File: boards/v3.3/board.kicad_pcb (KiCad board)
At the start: 2 copper layers, 96 x 91.4 mm, 63 parts, among them J1 KF301-2P, J2 KF301-2P, J3 KF301-2P, J4 KF301-2P, J5 KF301-2P, J6 KF301-2P, P1 Pin Header, P2 Pin Header, P3 Pin Header, P4 Pin Header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

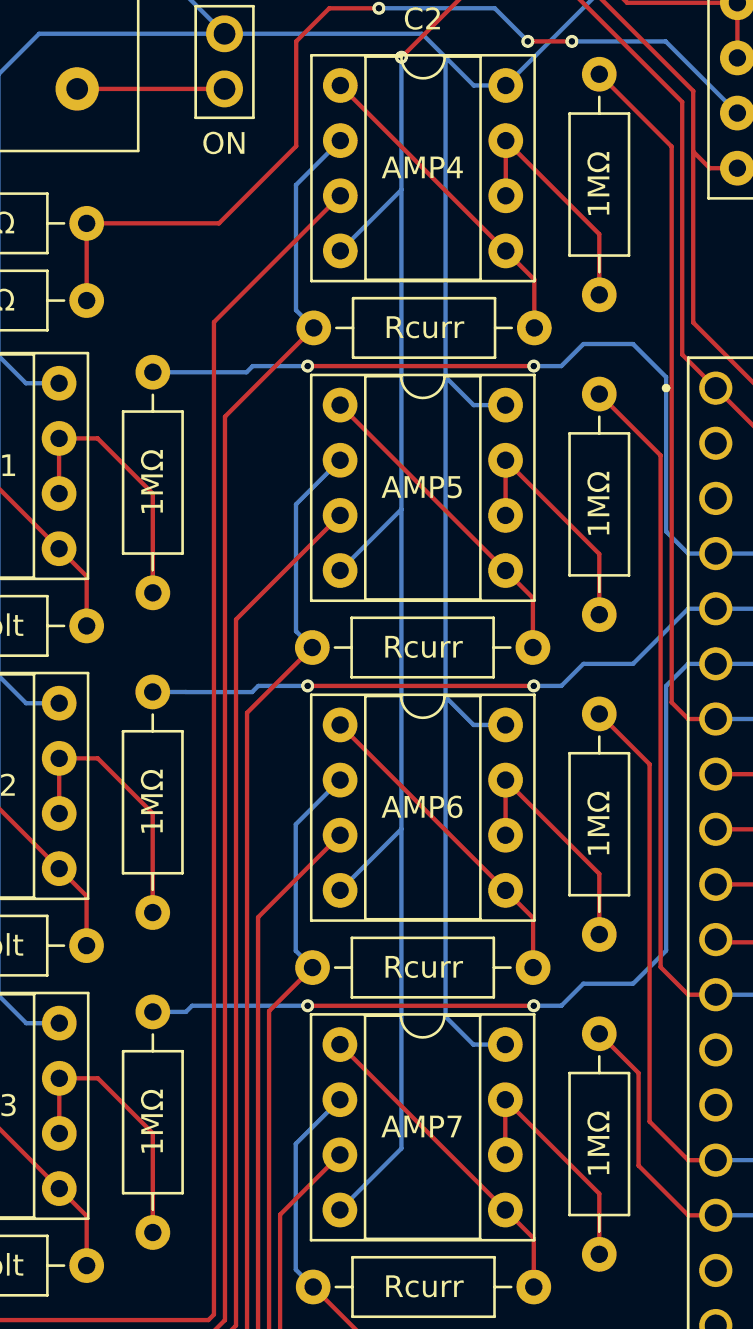
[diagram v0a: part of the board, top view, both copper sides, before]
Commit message: Update the list of components and calcs
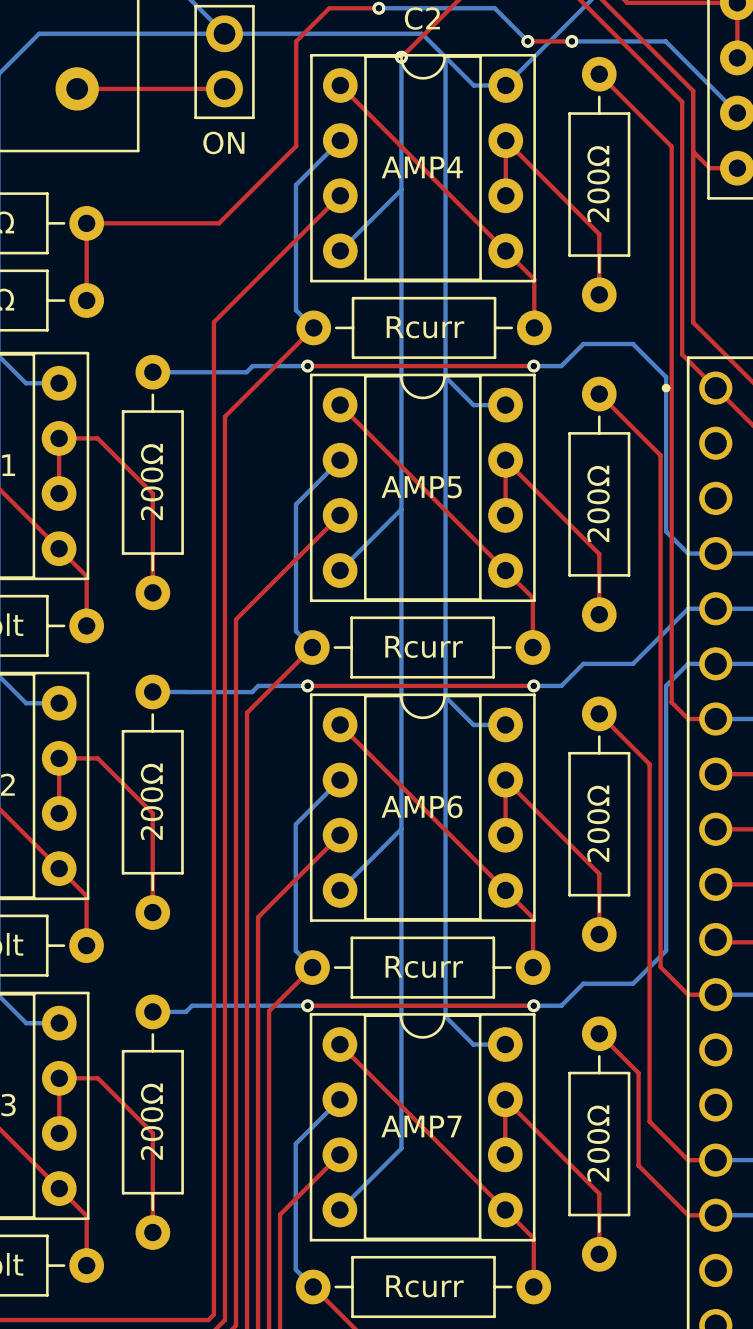
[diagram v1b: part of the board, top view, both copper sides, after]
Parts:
- R13, R14, R15, R16, R17, R18, R19: value 1MΩ -> 200Ω
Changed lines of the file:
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@@
     (title "Energy Guardian V3.3 PCI")
     (date "01/06/2024")
-    (rev "1.0")
+    (rev "1.1")
     (company "linkedin.com/in/lucasrguerra")
     (comment 1 "github.com/lucasrguerra/power_vision")
@@
         (effects (font (size 1 1) (thickness 0.15)))
     )
-    (fp_text value "1MΩ" (at 5.08 2.37 90) (layer "F.Fab") hide
+    (fp_text value "200Ω" (at 5.08 2.37 90) (layer "F.Fab") hide
         (effects (font (size 1 1) (thickness 0.15)))
     )
@@
         (effects (font (size 1 1) (thickness 0.15)))
     )
-    (fp_text value "1MΩ" (at 5.08 2.37 90) (layer "F.Fab") hide
+    (fp_text value "200Ω" (at 5.08 2.37 90) (layer "F.Fab") hide
         (effects (font (size 1 1) (thickness 0.15)))
     )
@@
         (effects (font (size 1 1) (thickness 0.15)))
     )
-    (fp_text value "1MΩ" (at 5.08 2.37 90) (layer "F.Fab") hide
+    (fp_text value "200Ω" (at 5.08 2.37 90) (layer "F.Fab") hide
         (effects (font (size 1 1) (thickness 0.15)))
     )
@@
         (effects (font (size 1 1) (thickness 0.15)))
     )
-    (fp_text value "1MΩ" (at 5.08 2.37 90) (layer "F.Fab") hide
+    (fp_text value "200Ω" (at 5.08 2.37 90) (layer "F.Fab") hide
         (effects (font (size 1 1) (thickness 0.15)))
     )
@@
         (effects (font (size 1 1) (thickness 0.15)))
     )
-    (fp_text value "1MΩ" (at 5.08 2.37 90) (layer "F.Fab") hide
+    (fp_text value "200Ω" (at 5.08 2.37 90) (layer "F.Fab") hide
         (effects (font (size 1 1) (thickness 0.15)))
     )
@@
         (effects (font (size 1 1) (thickness 0.15)))
     )
-    (fp_text value "1MΩ" (at 5.08 2.37 90) (layer "F.Fab") hide
+    (fp_text value "200Ω" (at 5.08 2.37 90) (layer "F.Fab") hide
         (effects (font (size 1 1) (thickness 0.15)))
     )
@@
         (effects (font (size 1 1) (thickness 0.15)))
     )
-    (fp_text value "1MΩ" (at 5.08 2.37 90) (layer "F.Fab") hide
+    (fp_text value "200Ω" (at 5.08 2.37 90) (layer "F.Fab") hide
         (effects (font (size 1 1) (thickness 0.15)))
     )

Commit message: Update board v3.3
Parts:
- moved P2 0.25 mm to (161.3, 56.9)
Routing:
- net TP B-1: track 17.3 -> 18.5 mm
- net MISO: track 33.0 -> 32.3 mm, vias 2 -> 1
- net Vcc: track 157.8 -> 158.4 mm
- net GND: track 319.4 -> 320.0 mm
- net CS: track 35.4 -> 34.8 mm, vias 2 -> 1

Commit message: Add the earth plan in the v3.3 board
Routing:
- net GND: track 320.0 -> 0.18 mm, vias 1 -> 0
- net Vcc: track 158.4 -> 172.2 mm
- added copper zone on B.Cu, net GND
- added copper zone on F.Cu, net GND

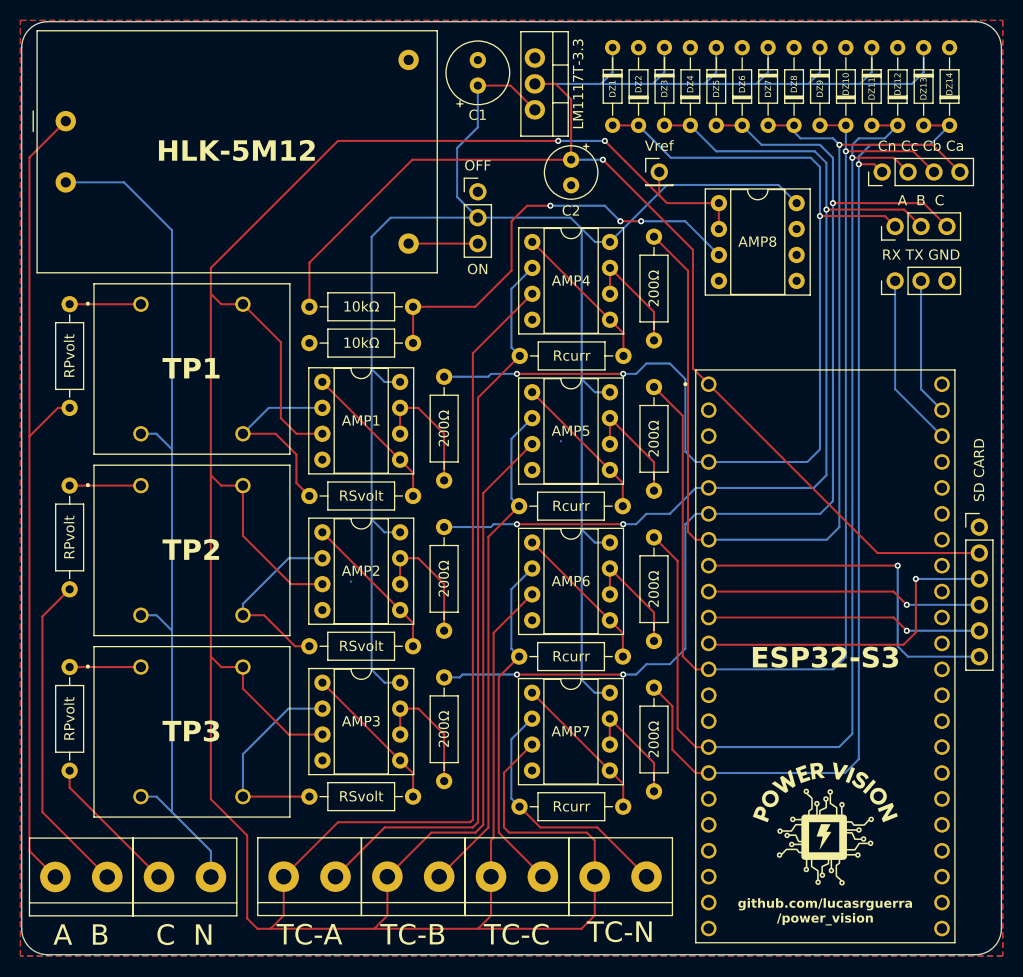
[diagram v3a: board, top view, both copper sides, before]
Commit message: Recalculation of load resistors
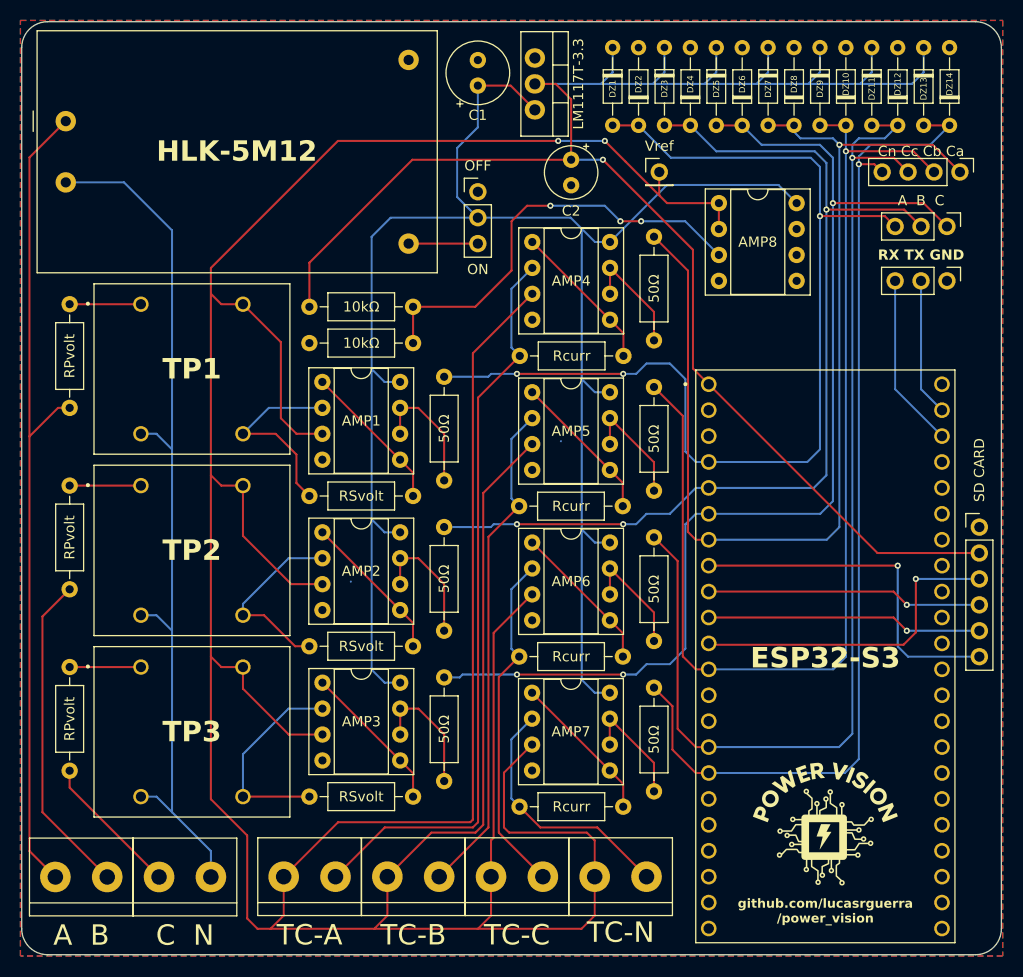
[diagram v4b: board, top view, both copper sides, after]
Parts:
- R13, R14, R15, R16, R17, R18, R19: value 200Ω -> 50Ω
- moved P3 7.62 mm to (190.8, 56.9), turned to -90 degrees
- moved P4 5.08 mm to (189.5, 62.2), turned to -90 degrees
- moved P1 5.08 mm to (189.5, 67.6), turned to -90 degrees
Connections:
- P1 pad 1: UART RX -> GND
- P1 pad 3: GND -> UART RX
- P3 pad 1: Current N -> Current A
- P3 pad 2: Current C -> Current B
- P3 pad 3: Current B -> Current C
- P3 pad 4: Current A -> Current N
- P4 pad 1: Wave A -> Wave C
- P4 pad 3: Wave C -> Wave A

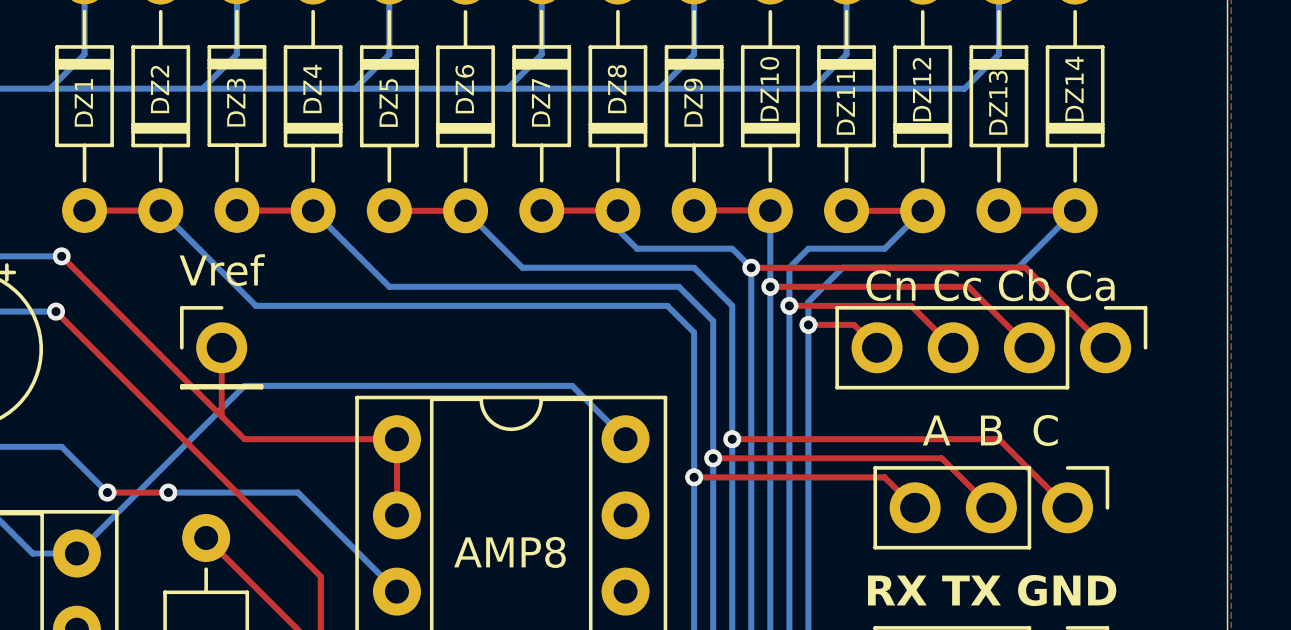
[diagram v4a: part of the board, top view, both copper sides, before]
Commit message: Correction on the board v3.3 silkscreen
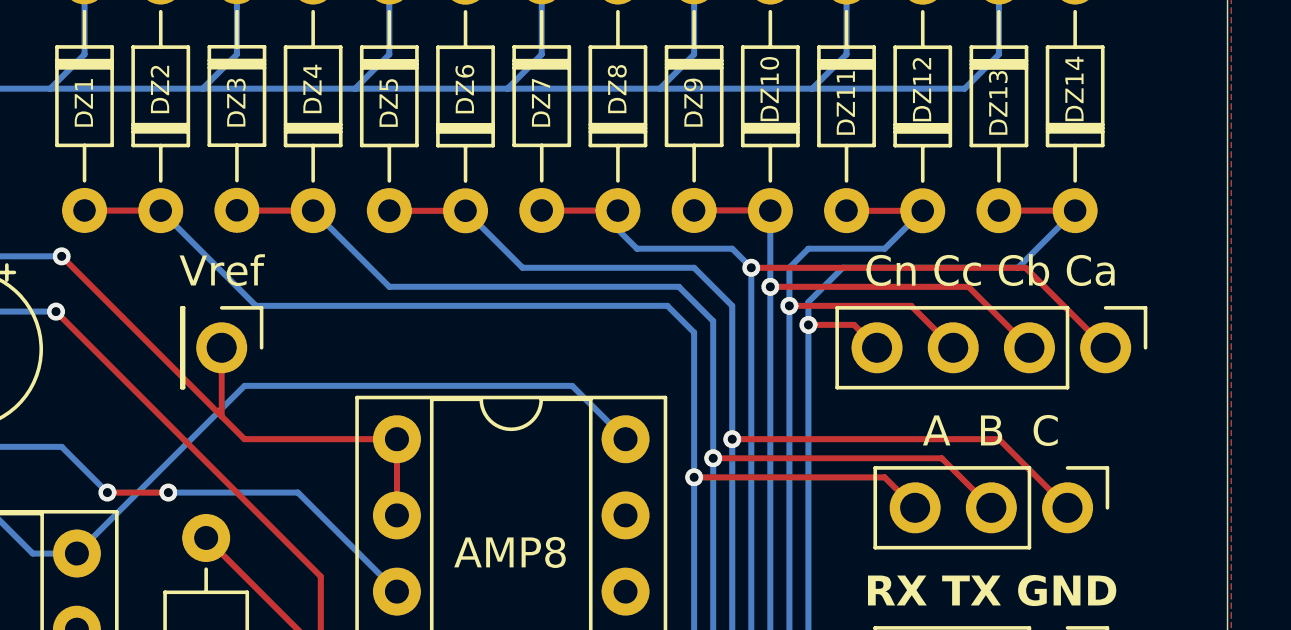
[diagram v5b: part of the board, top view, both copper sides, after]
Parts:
- turned P2 to -90 degrees
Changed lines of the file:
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@@
         (effects (font (size 1 1) (thickness 0.15)))
     )
-    (fp_text user "Cn Cc Cb Ca" (at -2.032 3.811) (layer "F.SilkS")
+    (fp_text user "Cn Cc Cb Ca" (at -2.54 3.811) (layer "F.SilkS")
         (effects (font (size 1 1) (thickness 0.2)))
     )
@@
   )
   (footprint "Connector_PinHeader_2.54mm:PinHeader_1x01_P2.54mm_Vertical" (layer "F.Cu")
-    (at 161.29 56.896)
+    (at 161.29 56.896 -90)
     (descr "Through hole straight pin header, 1x01, 2.54mm pitch, single row")
     (tags "Through hole pin header THT 1x01 2.54mm single row")
@@
     (property "ki_keywords" "connector")
     (attr through_hole)
-    (fp_text reference "P2" (at 0 -2.33) (layer "F.Fab") hide
-        (effects (font (size 1 1) (thickness 0.15)))
-    )
-    (fp_text value "Pin Header" (at 0 2.33) (layer "F.Fab") hide
-        (effects (font (size 1 1) (thickness 0.15)))
-    )
-    (fp_text user "Vref" (at 0 -2.54 180) (layer "F.SilkS")
+    (fp_text reference "P2" (at 0 -2.33 90) (layer "F.Fab") hide
+        (effects (font (size 1 1) (thickness 0.15)))
+    )
+    (fp_text value "Pin Header" (at 0 2.33 90) (layer "F.Fab") hide
+        (effects (font (size 1 1) (thickness 0.15)))
+    )
+    (fp_text user "Vref" (at -2.54 0 -180) (layer "F.SilkS")
         (effects (font (size 1 1) (thickness 0.2)))
     )
@@
     (fp_line (start 1.27 1.27) (end -1.27 1.27)
       (stroke (width 0.1) (type solid)) (layer "F.Fab"))
-    (pad "1" thru_hole oval (at 0 0) (size 1.7 1.7) (drill 1) (layers "*.Cu" "*.Mask")
+    (pad "1" thru_hole oval (at 0 0 270) (size 1.7 1.7) (drill 1) (layers "*.Cu" "*.Mask")
       (net 15 "TC A-1") (pinfunction "Pin_1") (pintype "passive"))
     (model "${KICAD6_3DMODEL_DIR}/Connector_PinHeader_2.54mm.3dshapes/PinHeader_1x01_P2.54mm_Vertical.wrl"
